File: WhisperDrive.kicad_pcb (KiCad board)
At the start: 2 copper layers, 86.6 x 70 mm, 22 parts, among them J1 VFAN1 Enable, J2 FAN1_BYPASS, J4 Power In, J5 Fan 1, Q1 25N06, U1 RP2040-Zero

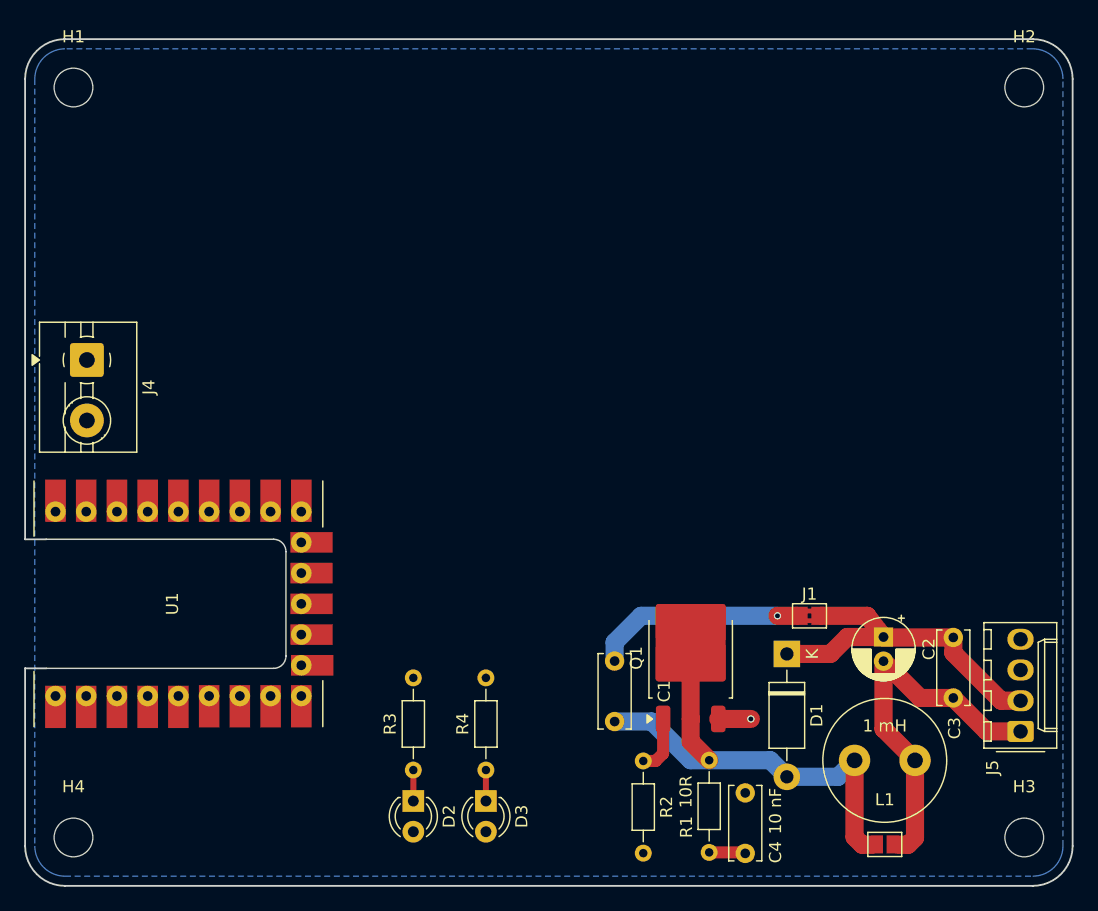
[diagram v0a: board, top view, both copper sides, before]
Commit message: DangerKlipper is Kalico now. + More changes not committed in the last commit. Oopsie.
Signed-off-by: HumbleDeer <djsndcx@gmail.com>
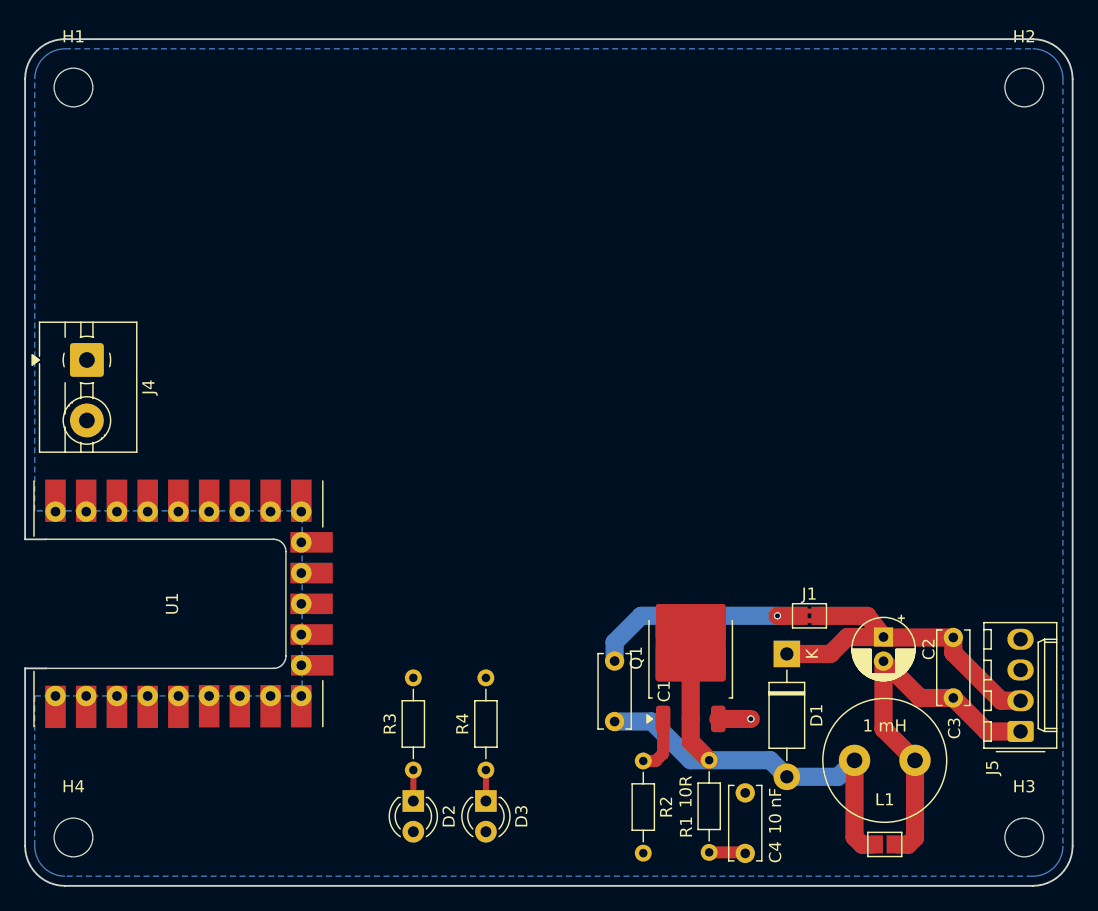
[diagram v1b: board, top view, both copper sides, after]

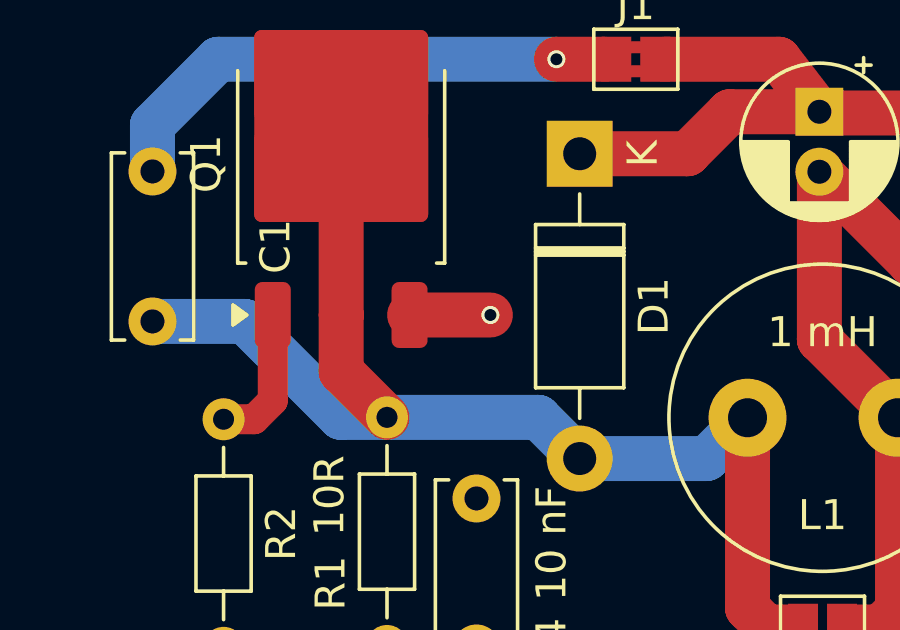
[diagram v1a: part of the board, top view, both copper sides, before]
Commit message: added: gate driver, second circuit, regulator for driver, optional separate power rail for fan/drive modified: changed global labels to net labels, moved power circuitry to subsheet
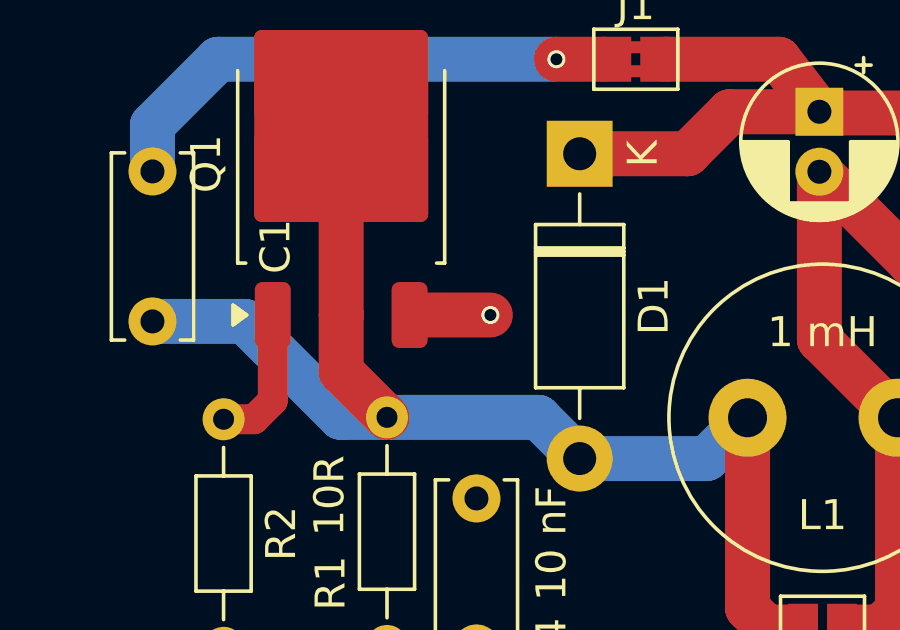
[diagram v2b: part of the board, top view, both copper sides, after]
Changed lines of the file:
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@@
 	)
 	(segment
-		(start 177.305 134.6)
+		(start 177.5 134.6)
 		(end 180 134.6)
 		(width 1.5)
